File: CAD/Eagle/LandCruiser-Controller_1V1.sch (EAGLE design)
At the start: 65 parts, among them IC611 LM7805, K311 V23086C1001A403, K312 V23086C1001A403, K313 V23086C1001A403, K314 V23086C1001A403, K315 V23086C1001A403, U101 MEGA8-P, U221 SN75240, U301 MIC2981/2982SO18W, U501 MAX232_SOIC16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

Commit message: HW_V1.1 - driver switches against ground, not Vbat. Another input line added.
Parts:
- added R121: 4k7R, rcl:R-EU_R0805
- added R321: 56R, rcl:R-EU_R0805
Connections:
- new net MP_SH_G: R124.1, R321.1, U101.PB0(ICP)
- new net SH_G: R321.2, X321.8
- net +12V: no longer D311.C, D312.C, D313.C, D314.C, D315.C, K3111.1, K3121.1, K3131.1, K3141.1, K3151.1
- net +5V: now also R121.2, R123.2, R124.2, R125.1, R126.1; no longer R123.1, R124.1, R125.2, R126.2
- net DRV_KL: now also D311.C; no longer D311.A
- net DRV_M1: now also D314.C; no longer D314.A
- net DRV_M2: now also D315.C; no longer D315.A
- net DRV_PV_G: now also D312.C; no longer D312.A
- net DRV_PV_O: now also D313.C; no longer D313.A
- net GND: now also D311.A, D312.A, D313.A, D314.A, D315.A, K3111.1, K3121.1, K3131.1, K3141.1, K3151.1; no longer X321.8
- net MP_FB: now also R121.1; no longer R122.1
- net MP_SA_G: now also R122.1; no longer R125.1
- net MP_SA_O: now also R123.1; no longer R126.1
- net MP_SK_G: now also R125.2; no longer R123.2
- net MP_SK_O: now also R126.2; no longer R124.2
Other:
- note added: "PCINT10"
- moved on the sheet: D141, D311, D312, D313, D314, D315, R123, R124, R125, R126, R131, R132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

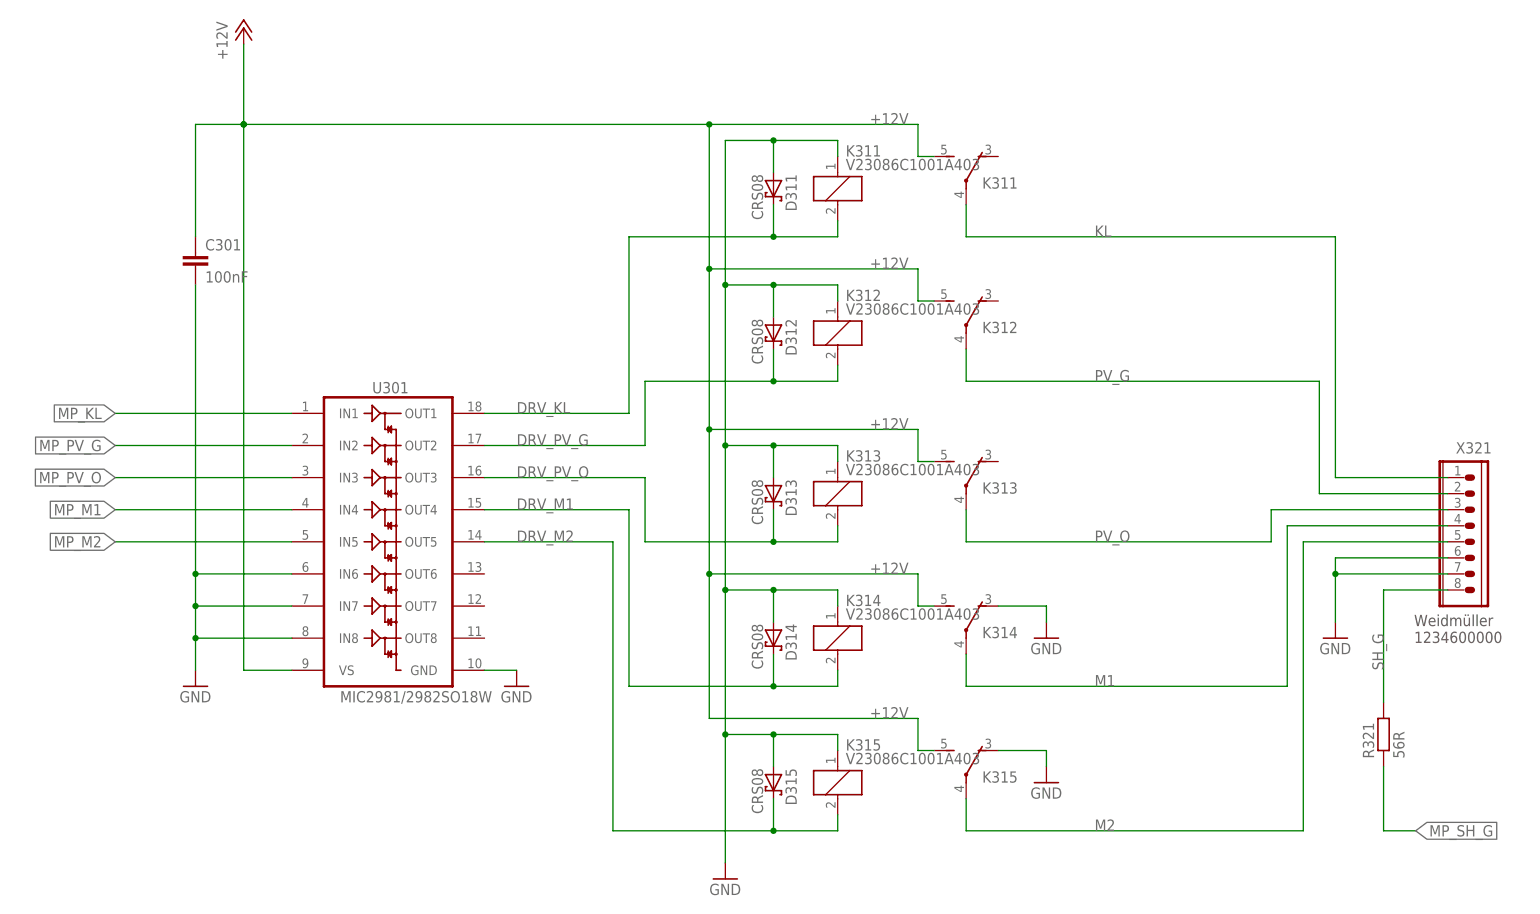
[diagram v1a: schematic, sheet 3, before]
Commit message: HW_V1.1 - switched FB input with rear tail gate (SH_G)
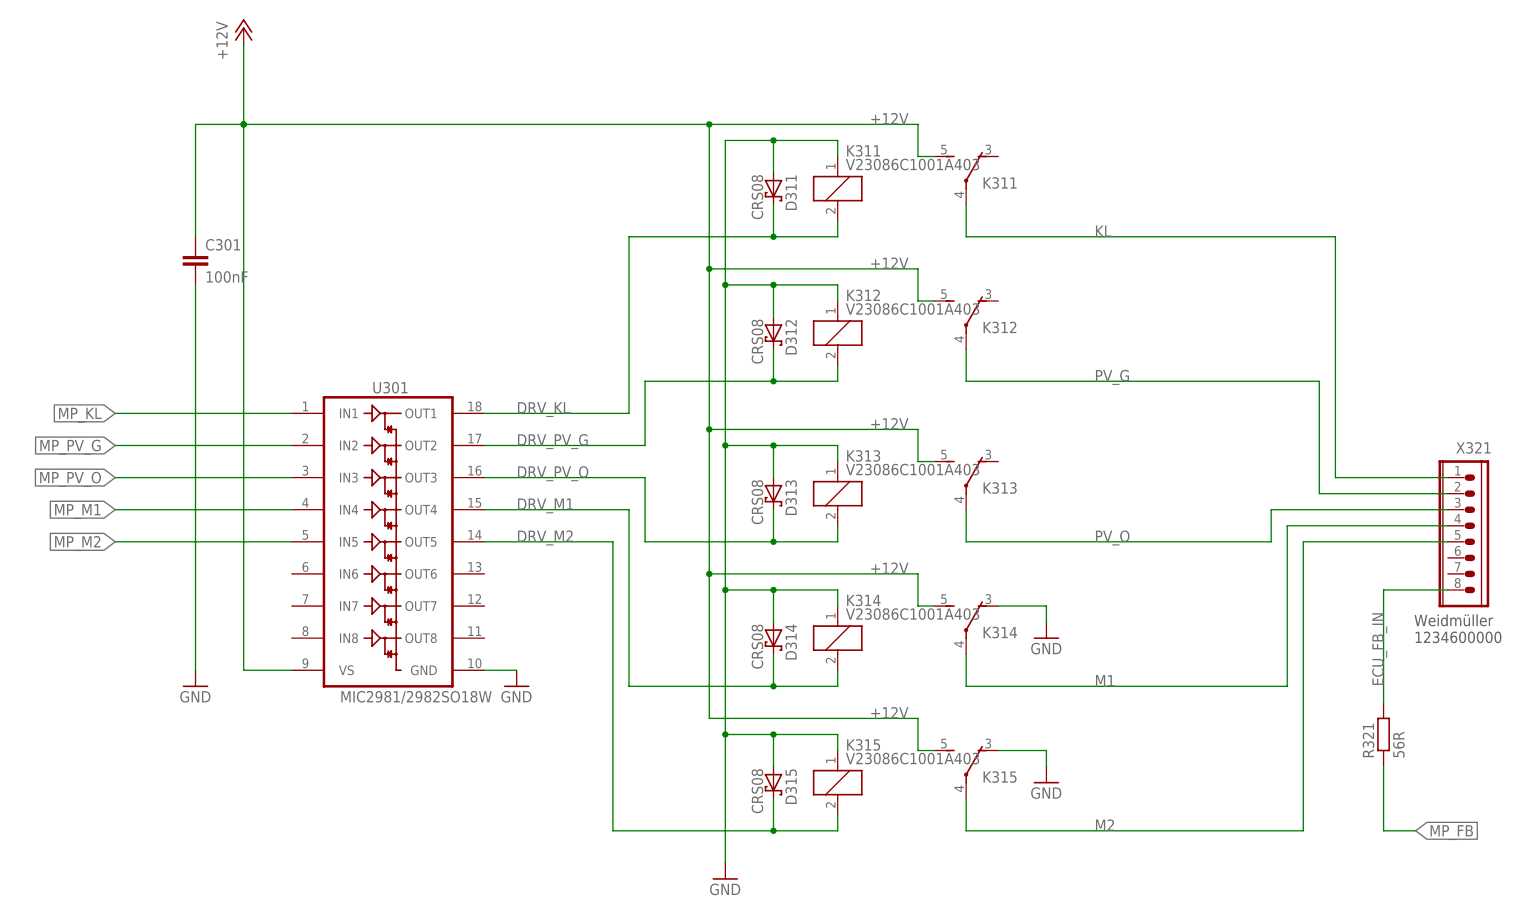
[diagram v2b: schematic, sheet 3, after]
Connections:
- removed net ECU_FB: R212.1, X201.2
- new net ECU_FB_IN: R321.2, X321.8
- net GND: no longer U301.IN6, U301.IN7, U301.IN8, X321.6, X321.7
- net MP_FB: now also R124.1, R321.1, U101.PB0(ICP); no longer R121.1, R212.2, U101.PD4(XCK/T0)
- net MP_SH_G: now also R121.1, R212.2, U101.PD4(XCK/T0); no longer R124.1, R321.1, U101.PB0(ICP)
- net SH_G: now also R212.1, X201.2; no longer R321.2, X321.8
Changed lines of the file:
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@@
 <part name="SUPPLY_601" library="df4iah_supply" deviceset="+UB" device=""/>
 <part name="X321" library="df4iah_connector" deviceset="WIRE-TO-BOARD_5MM08_1X08" device="" value="WEIDMUELLER 1234600000"/>
-<part name="GND321" library="df4iah_supply" deviceset="GND" device=""/>
 <part name="D601" library="df4iah_diode" deviceset="CRS08" device=""/>
 <part name="U221" library="df4iah_esd" deviceset="SN75240" device=""/>
@@
 </segment>
 </net>
-<net name="MP_FB" class="0">
-<segment>
-<pinref part="U101" gate="G$1" pin="PD4(XCK/T0)"/>
-<wire x1="160.02" y1="86.36" x2="170.18" y2="86.36" width="0.1524" layer="91"/>
-<wire x1="170.18" y1="86.36" x2="170.18" y2="30.48" width="0.1524" layer="91"/>
-<wire x1="170.18" y1="30.48" x2="58.42" y2="30.48" width="0.1524" layer="91"/>
-<label x="33.02" y="30.48" size="1.778" layer="95" rot="R180" xref="yes"/>
-<pinref part="R121" gate="G$1" pin="1"/>
-<wire x1="58.42" y1="30.48" x2="33.02" y2="30.48" width="0.1524" layer="91"/>
-<wire x1="58.42" y1="45.72" x2="58.42" y2="30.48" width="0.1524" layer="91"/>
-<junction x="58.42" y="30.48"/>
-</segment>
-</net>
 <net name="MP_SK_O" class="0">
 <segment>
@@
 </segment>
 </net>
-<net name="MP_SH_G" class="0">
+<net name="MP_FB" class="0">
 <segment>
 <wire x1="162.56" y1="38.1" x2="88.9" y2="38.1" width="0.1524" layer="91"/>
 <label x="33.02" y="38.1" size="1.778" layer="95" rot="R180" xref="yes"/>
-<pinref part="R124" gate="G$1" pin="1"/>
 <wire x1="88.9" y1="38.1" x2="33.02" y2="38.1" width="0.1524" layer="91"/>
-<wire x1="88.9" y1="45.72" x2="88.9" y2="38.1" width="0.1524" layer="91"/>
 <junction x="88.9" y="38.1"/>
 <pinref part="U101" gate="G$1" pin="PB0(ICP)"/>
 <wire x1="160.02" y1="73.66" x2="162.56" y2="73.66" width="0.1524" layer="91"/>
 <wire x1="162.56" y1="73.66" x2="162.56" y2="38.1" width="0.1524" layer="91"/>
+<pinref part="R124" gate="G$1" pin="1"/>
+<wire x1="88.9" y1="38.1" x2="88.9" y2="45.72" width="0.1524" layer="91"/>
+</segment>
+</net>
+<net name="MP_SH_G" class="0">
+<segment>
+<pinref part="U101" gate="G$1" pin="PD4(XCK/T0)"/>
+<wire x1="160.02" y1="86.36" x2="170.18" y2="86.36" width="0.1524" layer="91"/>
+<wire x1="170.18" y1="86.36" x2="170.18" y2="30.48" width="0.1524" layer="91"/>
+<wire x1="170.18" y1="30.48" x2="58.42" y2="30.48" width="0.1524" layer="91"/>
+<label x="33.02" y="30.48" size="1.778" layer="95" rot="R180" xref="yes"/>
+<wire x1="58.42" y1="30.48" x2="33.02" y2="30.48" width="0.1524" layer="91"/>
+<junction x="58.42" y="30.48"/>
+<pinref part="R121" gate="G$1" pin="1"/>
+<wire x1="58.42" y1="30.48" x2="58.42" y2="45.72" width="0.1524" layer="91"/>
 </segment>
 </net>
@@
 </busses>
 <nets>
-<net name="ECU_FB" class="0">
+<net name="SH_G" class="0">
 <segment>
 <wire x1="40.64" y1="96.52" x2="40.64" y2="129.54" width="0.1524" layer="91"/>
@@
 <wire x1="205.74" y1="83.82" x2="205.74" y2="81.28" width="0.1524" layer="91"/>
 <junction x="205.74" y="81.28"/>
-</segment>
-</net>
-<net name="MP_FB" class="0">
-<segment>
-<pinref part="R212" gate="G$1" pin="2"/>
-<wire x1="83.82" y1="129.54" x2="215.9" y2="129.54" width="0.1524" layer="91"/>
-<label x="215.9" y="129.54" size="1.778" layer="95" xref="yes"/>
 </segment>
 </net>
@@
 <wire x1="127" y1="170.18" x2="127" y2="167.64" width="0.1524" layer="91"/>
 <label x="55.88" y="170.18" size="1.778" layer="95"/>
+</segment>
+</net>
+<net name="MP_SH_G" class="0">
+<segment>
+<pinref part="R212" gate="G$1" pin="2"/>
+<wire x1="83.82" y1="129.54" x2="215.9" y2="129.54" width="0.1524" layer="91"/>
+<label x="215.9" y="129.54" size="1.778" layer="95" xref="yes"/>
 </segment>
 </net>
@@
 <instance part="FRAME6" gate="G$1" x="0" y="0"/>
 <instance part="X321" gate="G$1" x="241.3" y="91.44"/>
-<instance part="GND321" gate="1" x="220.98" y="73.66"/>
 <instance part="U301" gate="G$1" x="71.12" y="96.52"/>
 <instance part="GND302" gate="1" x="91.44" y="66.04"/>
@@
 <net name="GND" class="0">
 <segment>
-<pinref part="GND321" gate="1" pin="GND"/>
-<wire x1="220.98" y1="76.2" x2="220.98" y2="83.82" width="0.1524" layer="91"/>
-<pinref part="X321" gate="G$1" pin="7"/>
-<wire x1="220.98" y1="83.82" x2="238.76" y2="83.82" width="0.1524" layer="91"/>
-<wire x1="220.98" y1="83.82" x2="220.98" y2="86.36" width="0.1524" layer="91"/>
-<junction x="220.98" y="83.82"/>
-<pinref part="X321" gate="G$1" pin="6"/>
-<wire x1="220.98" y1="86.36" x2="238.76" y2="86.36" width="0.1524" layer="91"/>
-</segment>
-<segment>
 <pinref part="U301" gate="G$1" pin="GND"/>
 <wire x1="86.36" y1="68.58" x2="91.44" y2="68.58" width="0.1524" layer="91"/>
@@
 <segment>
 <pinref part="GND301" gate="1" pin="GND"/>
-<wire x1="40.64" y1="68.58" x2="40.64" y2="73.66" width="0.1524" layer="91"/>
-<pinref part="U301" gate="G$1" pin="IN6"/>
-<wire x1="40.64" y1="73.66" x2="40.64" y2="78.74" width="0.1524" layer="91"/>
-<wire x1="40.64" y1="78.74" x2="40.64" y2="83.82" width="0.1524" layer="91"/>
-<wire x1="40.64" y1="83.82" x2="55.88" y2="83.82" width="0.1524" layer="91"/>
-<pinref part="U301" gate="G$1" pin="IN7"/>
-<wire x1="40.64" y1="78.74" x2="55.88" y2="78.74" width="0.1524" layer="91"/>
-<junction x="40.64" y="78.74"/>
-<pinref part="U301" gate="G$1" pin="IN8"/>
-<wire x1="40.64" y1="73.66" x2="55.88" y2="73.66" width="0.1524" layer="91"/>
-<junction x="40.64" y="73.66"/>
 <pinref part="C301" gate="G$1" pin="2"/>
-<wire x1="40.64" y1="129.54" x2="40.64" y2="83.82" width="0.1524" layer="91"/>
-<junction x="40.64" y="83.82"/>
+<wire x1="40.64" y1="129.54" x2="40.64" y2="68.58" width="0.1524" layer="91"/>
 </segment>
 <segment>
@@
 </segment>
 </net>
-<net name="MP_SH_G" class="0">
+<net name="ECU_FB_IN" class="0">
+<segment>
+<pinref part="R321" gate="G$1" pin="2"/>
+<wire x1="228.6" y1="63.5" x2="228.6" y2="81.28" width="0.1524" layer="91"/>
+<pinref part="X321" gate="G$1" pin="8"/>
+<wire x1="228.6" y1="81.28" x2="238.76" y2="81.28" width="0.1524" layer="91"/>
+<label x="228.6" y="66.04" size="1.778" layer="95" rot="R90"/>
+</segment>
+</net>
+<net name="MP_FB" class="0">
 <segment>
 <wire x1="228.6" y1="53.34" x2="228.6" y2="43.18" width="0.1524" layer="91"/>
@@
 </segment>
 </net>
-<net name="SH_G" class="0">
-<segment>
-<pinref part="R321" gate="G$1" pin="2"/>
-<wire x1="228.6" y1="63.5" x2="228.6" y2="81.28" width="0.1524" layer="91"/>
-<pinref part="X321" gate="G$1" pin="8"/>
-<wire x1="228.6" y1="81.28" x2="238.76" y2="81.28" width="0.1524" layer="91"/>
-<label x="228.6" y="68.58" size="1.778" layer="95" rot="R90"/>
-</segment>
-</net>
